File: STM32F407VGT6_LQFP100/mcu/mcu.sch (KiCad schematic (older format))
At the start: 12 parts, among them SW1 SW_Push, U1 STM32F407VGT6

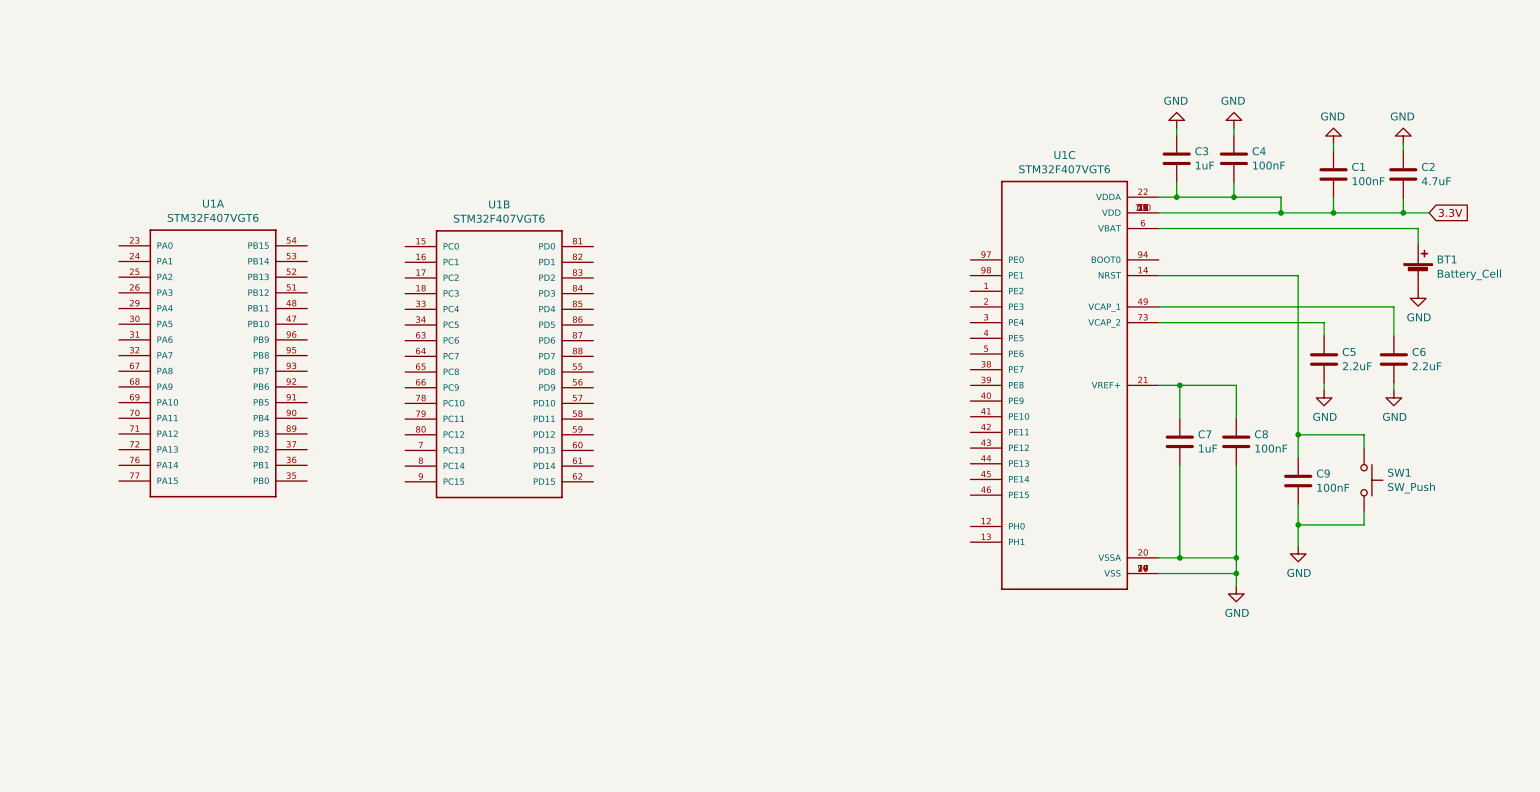
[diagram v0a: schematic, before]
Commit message: add oscillator
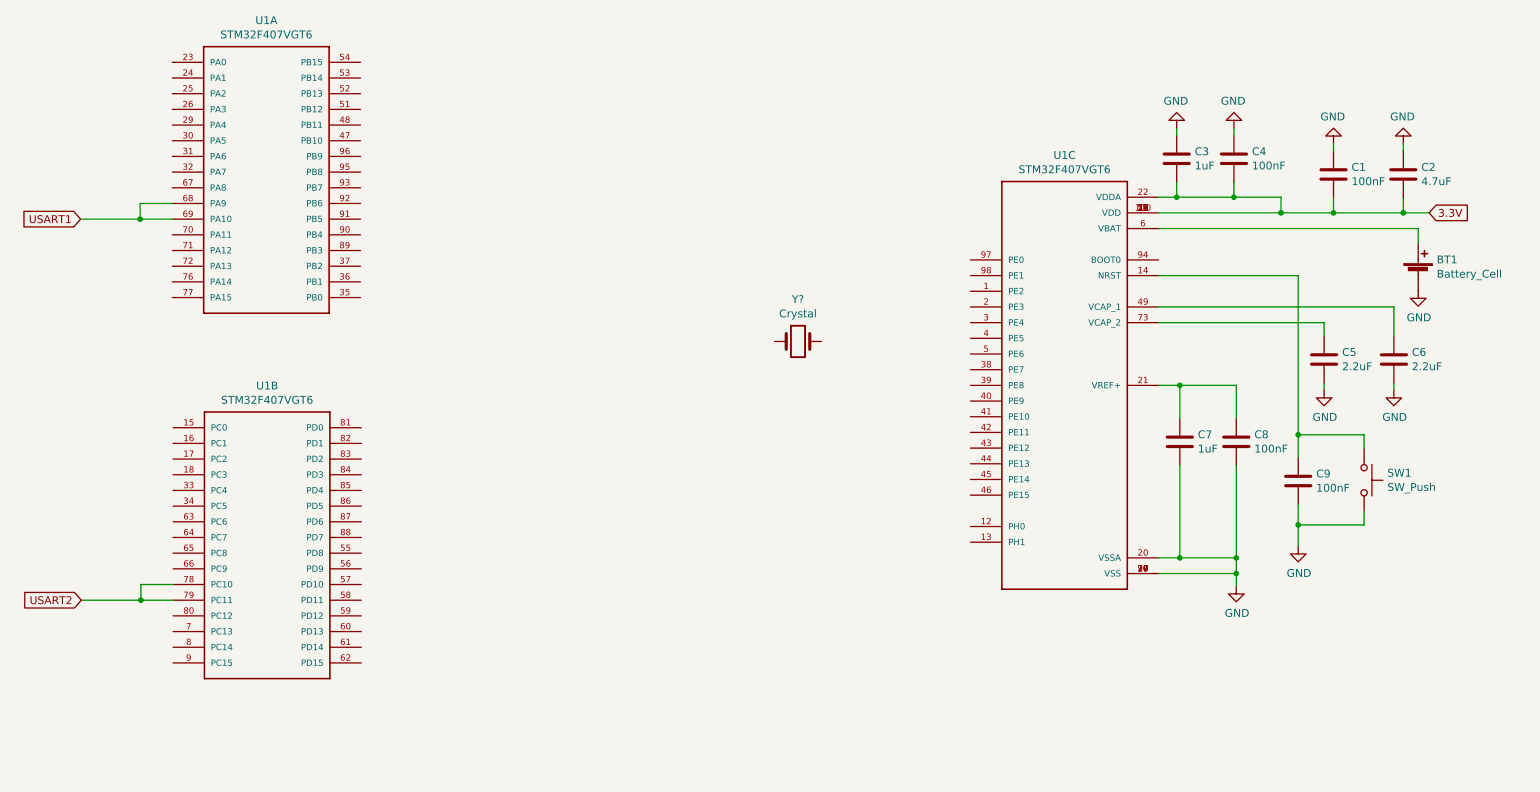
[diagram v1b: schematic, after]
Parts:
- added Y?: Crystal, symbol Device:Crystal
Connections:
- net USART1: now reaches U1.68 (PA9)
- net USART1: now also U1.69 (PA10)
- net USART2: now reaches U1.78 (PC10)
- net USART2: now also U1.79 (PC11)
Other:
- moved on the sheet: U1A, U1B
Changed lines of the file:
@@
 L STM32F407VGT6:STM32F407VGT6 U1
 U 2 1 5F49D5A0
-P 4565 3520
-F 0 "U1" H 4565 4587 50  0000 C CNN
-F 1 "STM32F407VGT6" H 4565 4496 50  0000 C CNN
-F 2 "QFP50P1600X1600X160-100N" H 4565 3520 50  0001 L BNN
-F 3 "" H 4565 3520 50  0001 L BNN
-F 4 "1.6mm" H 4565 3520 50  0001 L BNN "Field4"
-F 5 "ST Microelectronics" H 4565 3520 50  0001 L BNN "Field5"
-F 6 "8" H 4565 3520 50  0001 L BNN "Field6"
-	2    4565 3520
+P 3085 4675
+F 0 "U1" H 3085 5742 50  0000 C CNN
+F 1 "STM32F407VGT6" H 3085 5651 50  0000 C CNN
+F 2 "QFP50P1600X1600X160-100N" H 3085 4675 50  0001 L BNN
+F 3 "" H 3085 4675 50  0001 L BNN
+F 4 "1.6mm" H 3085 4675 50  0001 L BNN "Field4"
+F 5 "ST Microelectronics" H 3085 4675 50  0001 L BNN "Field5"
+F 6 "8" H 3085 4675 50  0001 L BNN "Field6"
+	2    3085 4675
 	1    0    0    -1
 $EndComp
@@
 L STM32F407VGT6:STM32F407VGT6 U1
 U 1 1 5F49A572
-P 2740 3515
-F 0 "U1" H 2740 4582 50  0000 C CNN
-F 1 "STM32F407VGT6" H 2740 4491 50  0000 C CNN
-F 2 "QFP50P1600X1600X160-100N" H 2740 3515 50  0001 L BNN
-F 3 "" H 2740 3515 50  0001 L BNN
-F 4 "1.6mm" H 2740 3515 50  0001 L BNN "Field4"
-F 5 "ST Microelectronics" H 2740 3515 50  0001 L BNN "Field5"
-F 6 "8" H 2740 3515 50  0001 L BNN "Field6"
-	1    2740 3515
+P 3080 2345
+F 0 "U1" H 3080 3412 50  0000 C CNN
+F 1 "STM32F407VGT6" H 3080 3321 50  0000 C CNN
+F 2 "QFP50P1600X1600X160-100N" H 3080 2345 50  0001 L BNN
+F 3 "" H 3080 2345 50  0001 L BNN
+F 4 "1.6mm" H 3080 2345 50  0001 L BNN "Field4"
+F 5 "ST Microelectronics" H 3080 2345 50  0001 L BNN "Field5"
+F 6 "8" H 3080 2345 50  0001 L BNN "Field6"
+	1    3080 2345
 	1    0    0    -1
 $EndComp
@@
 Wire Wire Line
 	9660 4495 9660 4630
+$Comp
+L Device:Crystal Y?
+U 1 1 5F5AB575
+P 6470 3325
+F 0 "Y?" H 6470 3593 50  0000 C CNN
+F 1 "Crystal" H 6470 3502 50  0000 C CNN
+F 2 "" H 6470 3325 50  0001 C CNN
+F 3 "~" H 6470 3325 50  0001 C CNN
+	1    6470 3325
+	1    0    0    -1
+$EndComp
+Wire Wire Line
+	2480 2545 2275 2545
+Wire Wire Line
+	2480 2445 2275 2445
+Wire Wire Line
+	2275 2445 2275 2545
+Text GLabel 1895 2545 0    50   Input ~ 0
+USART1
+Connection ~ 2275 2545
+Wire Wire Line
+	1895 2545 2275 2545
+Wire Wire Line
+	2485 4975 2280 4975
+Wire Wire Line
+	2485 4875 2280 4875
+Wire Wire Line
+	2280 4875 2280 4975
+Text GLabel 1900 4975 0    50   Input ~ 0
+USART2
+Connection ~ 2280 4975
+Wire Wire Line
+	1900 4975 2280 4975
 $EndSCHEMATC

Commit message: update
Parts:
- added C10, C9: 100nF, symbol Device:C
- added R1: R, symbol Device:R
- added R2: 10k, symbol Device:R
- added SW2: SW_Push, symbol Switch:SW_Push
- gave numbers to parts that had none: 1
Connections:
- net 3.3V: now also SW2.1
- net GND: now also C10.1, C9.2
- net at U1.12 (PH0): now also Y1.2, C9.1
- net at U1.13 (PH1): now also C10.2, R1.1
- net at U1.94 (BOOT0): now also R2.2
- net at Y1.1: now also R1.2
- new net: R2.1, SW2.2
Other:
- moved on the sheet: BT1, C1, C2, C3, C4, C5, C6, C7, C8, C9, SW1, U1A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
